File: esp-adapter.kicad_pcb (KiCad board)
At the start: 2 copper layers, 16 x 20.3 mm, 4 parts, among them J1 Conn_01x11_Male, J2 Conn_01x11_Male, J3 Conn_01x02_Male, U1 ESP-07

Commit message: thickness 1.0
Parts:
- moved J1 0.89 mm to (152.9, 107.4)
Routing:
- net 3V3: track 19.3 -> 31.1 mm, vias 3 -> 6
- net RXD0: track 23.2 -> 21.6 mm, vias 2 -> 3
- net GND: track 18.0 -> 19.1 mm, vias 3 -> 5
- net IO14: track 13.1 -> 13.9 mm, vias 2 -> 4
- net IO13: track 15.0 -> 14.6 mm, vias 1 -> 2
- net ADC: track 21.7 -> 22.0 mm, vias 1 -> 3
- net IO12: track 12.9 -> 13.1 mm, vias 2 -> 4
- net TXD0: track 26.7 -> 26.9 mm, vias 2 -> 3
- net RST: vias 1 -> 2
- net Net-(U1-Pad4): vias 1 -> 2
- net Net-(U1-Pad11): vias 1 -> 2
- net IO5: vias 1 -> 2
- net IO4: vias 1 -> 2
- net /PROG: vias 1 -> 2
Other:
- board size 16 x 20.3 mm -> 16 x 19.6 mm
- board text removed: "MAXIMUM PCB THICKNESS 0.8MM"

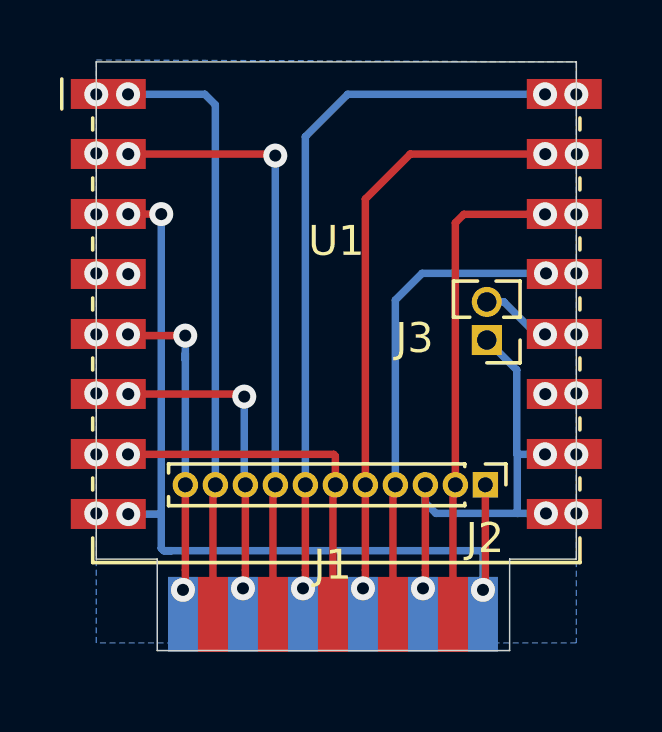
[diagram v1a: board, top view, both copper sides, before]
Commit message: no castelated holes
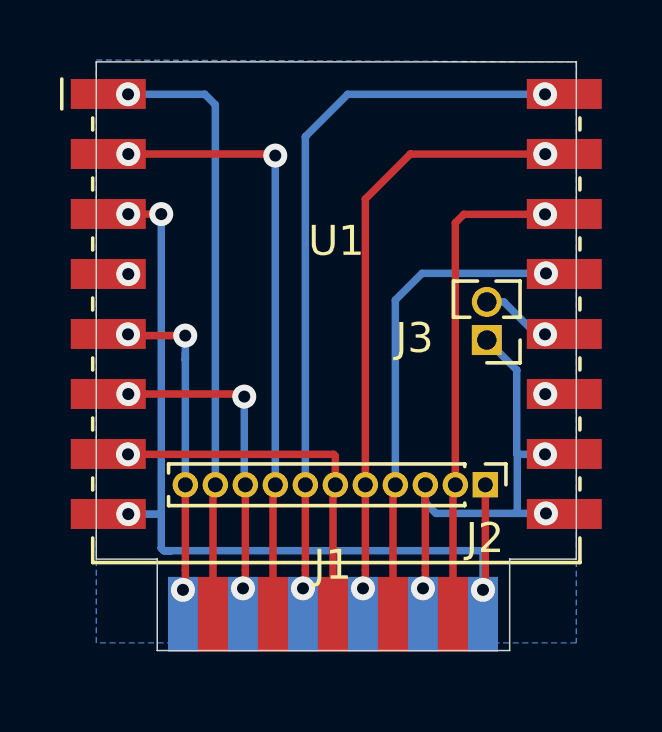
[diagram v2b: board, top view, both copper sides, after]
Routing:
- net TXD0: vias 3 -> 2
- net RXD0: vias 3 -> 2
- net RST: vias 2 -> 1
- net Net-(U1-Pad4): vias 2 -> 1
- net Net-(U1-Pad11): vias 2 -> 1
- net IO5: vias 2 -> 1
- net IO4: vias 2 -> 1
- net IO14: vias 4 -> 3
- net IO13: vias 2 -> 1
- net IO12: vias 4 -> 3
- net GND: vias 5 -> 3
- net ADC: vias 3 -> 2
- net 3V3: vias 6 -> 4
- net /PROG: vias 2 -> 1

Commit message: fabricated version
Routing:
- net GND: track 19.1 -> 17.8 mm
- net RST: track 22.2 -> 21.0 mm
- net IO14: track 13.9 -> 12.6 mm
- net IO13: track 14.6 -> 13.3 mm
- net TXD0: track 26.9 -> 25.7 mm
- net IO4: track 18.0 -> 16.8 mm
- net /PROG: track 3.08 -> 2.39 mm

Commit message: fix TX RX swap
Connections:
- U1 pad 15: RXD0 -> TXD0
- U1 pad 16: TXD0 -> RXD0
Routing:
- net RXD0: track 21.6 -> 24.0 mm
- net TXD0: track 25.7 -> 23.4 mm

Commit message: Revert "fix TX RX swap"
This reverts commit 031c61bf6d1d21104408cedd763a9be0f04462ce.
For explanation see issue #2 .
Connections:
- U1 pad 15: TXD0 -> RXD0
- U1 pad 16: RXD0 -> TXD0
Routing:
- net RXD0: track 24.0 -> 21.6 mm
- net TXD0: track 23.4 -> 25.7 mm
